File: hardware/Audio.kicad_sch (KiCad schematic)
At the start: 48 parts, among them IC1 LM4991xx, J4 CAT_TX, J6 CAT_TX, Q1 IRLML2060, Q2 BSS138, Q3 BSS138, U1 MAX9814, U201 MCP6002

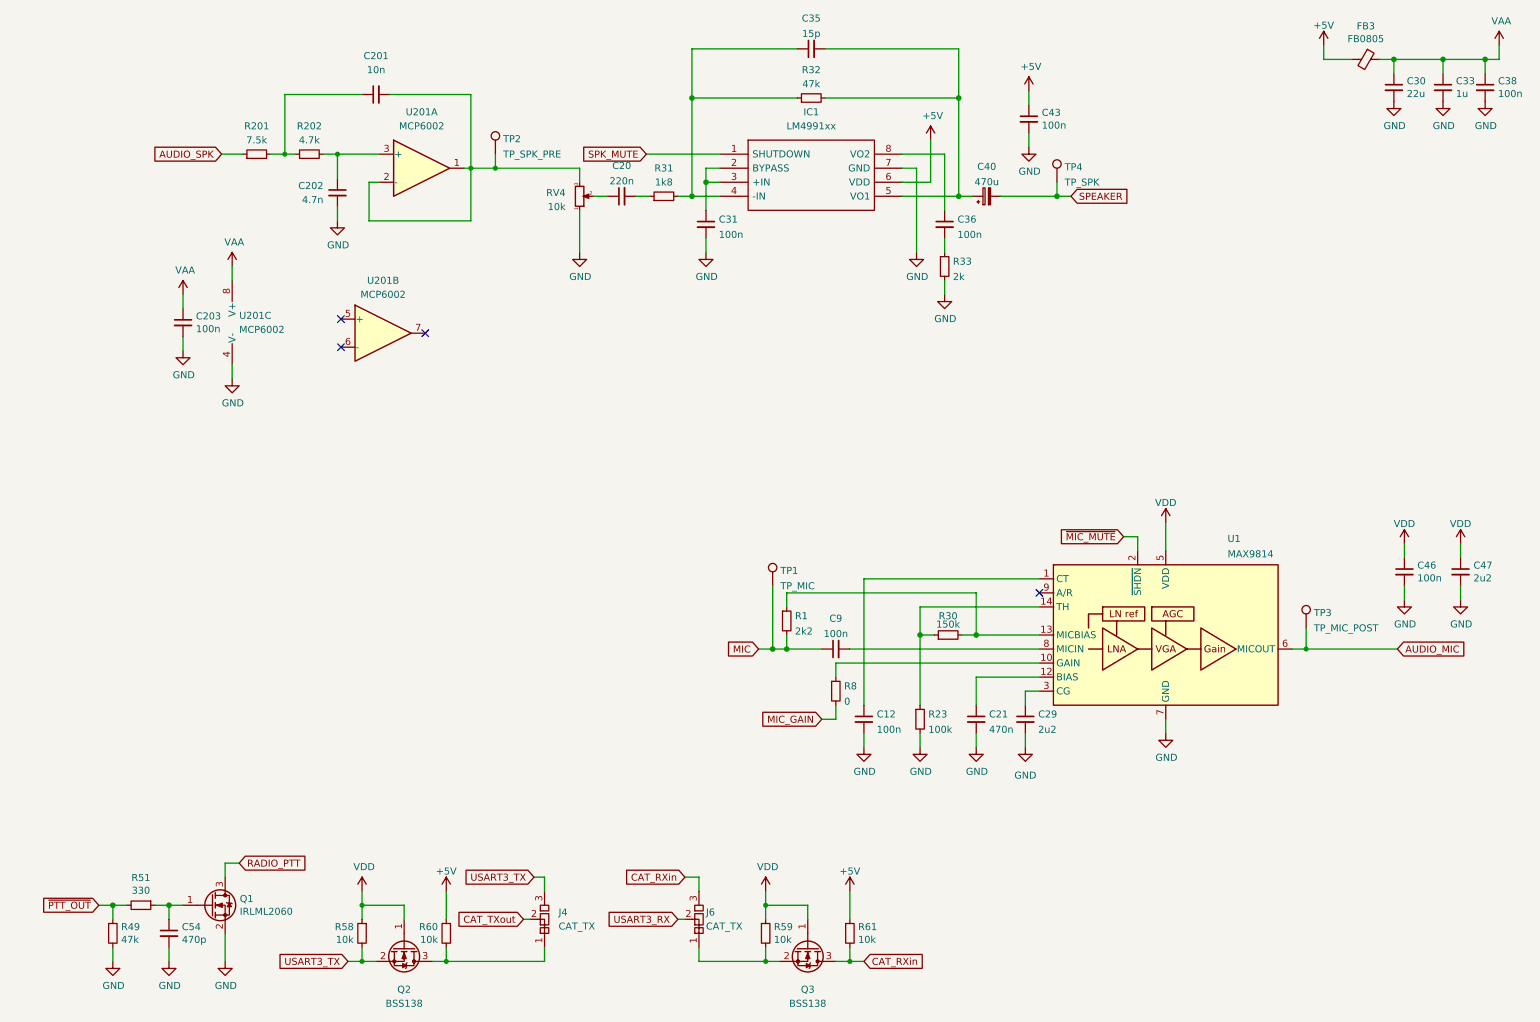
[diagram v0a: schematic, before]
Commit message: Reworked schematic
Rearranged disposition and renumbered components
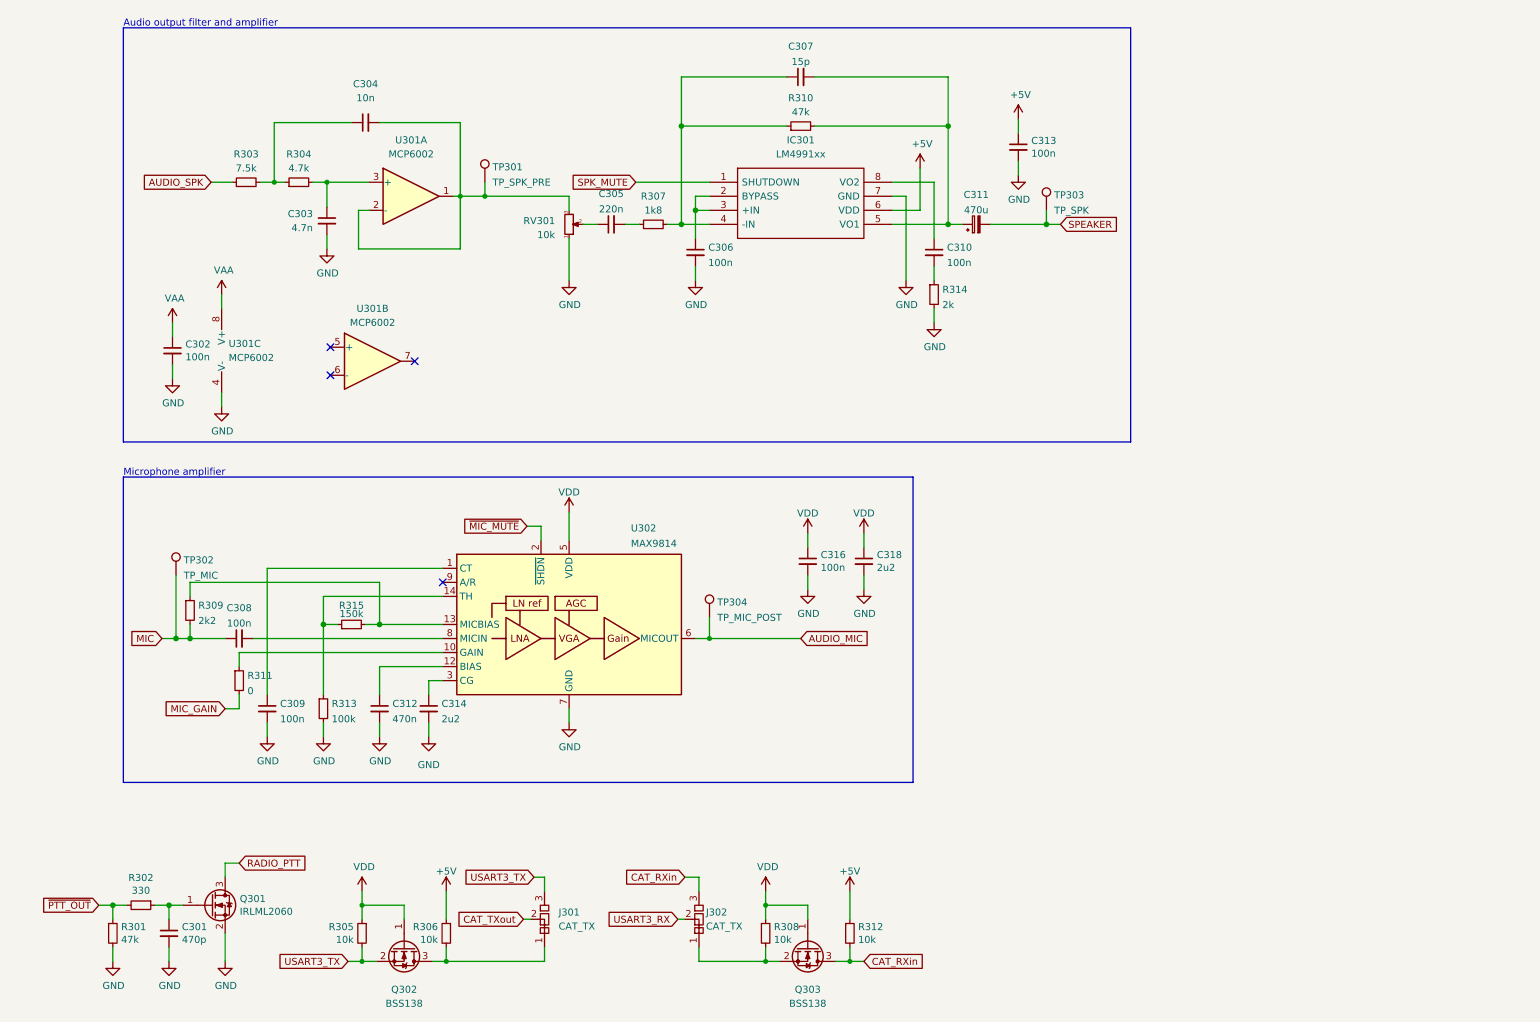
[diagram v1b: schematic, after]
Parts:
- removed C30: 22u, pkl_dipol:C_0603, symbol pkl_device:pkl_C_Small
- removed C33: 1u, pkl_dipol:C_0603, symbol pkl_device:pkl_C_Small
- removed C38: 100n, pkl_dipol:C_0603, symbol pkl_device:pkl_C_Small
- removed FB3: FB0805, pkl_dipol:L_0805, symbol Device:Ferrite_Bead_Small
- renumbered C54 to C301, C203 to C302, C202 to C303, C201 to C304, C20 to C305, C31 to C306, C35 to C307, C9 to C308, C12 to C309, C36 to C310, C40 to C311, C21 to C312, C43 to C313, C29 to C314, C46 to C316, C47 to C318, IC1 to IC301, J4 to J301, J6 to J302, Q1 to Q301, Q2 to Q302, Q3 to Q303, R49 to R301, R51 to R302, R201 to R303, R202 to R304, R58 to R305, R60 to R306, R31 to R307, R59 to R308, R1 to R309, R32 to R310, R8 to R311, R61 to R312, R23 to R313, R33 to R314, R30 to R315, RV4 to RV301, TP2 to TP301, TP1 to TP302, TP4 to TP303, TP3 to TP304, U201 to U301, U1 to U302
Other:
- note added: "Audio output filter and amplifier"
- note added: "Microphone amplifier"
- moved on the sheet: C302, C303, C304, C305, C306, C307, C308, C309, C310, C311, C312, C313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

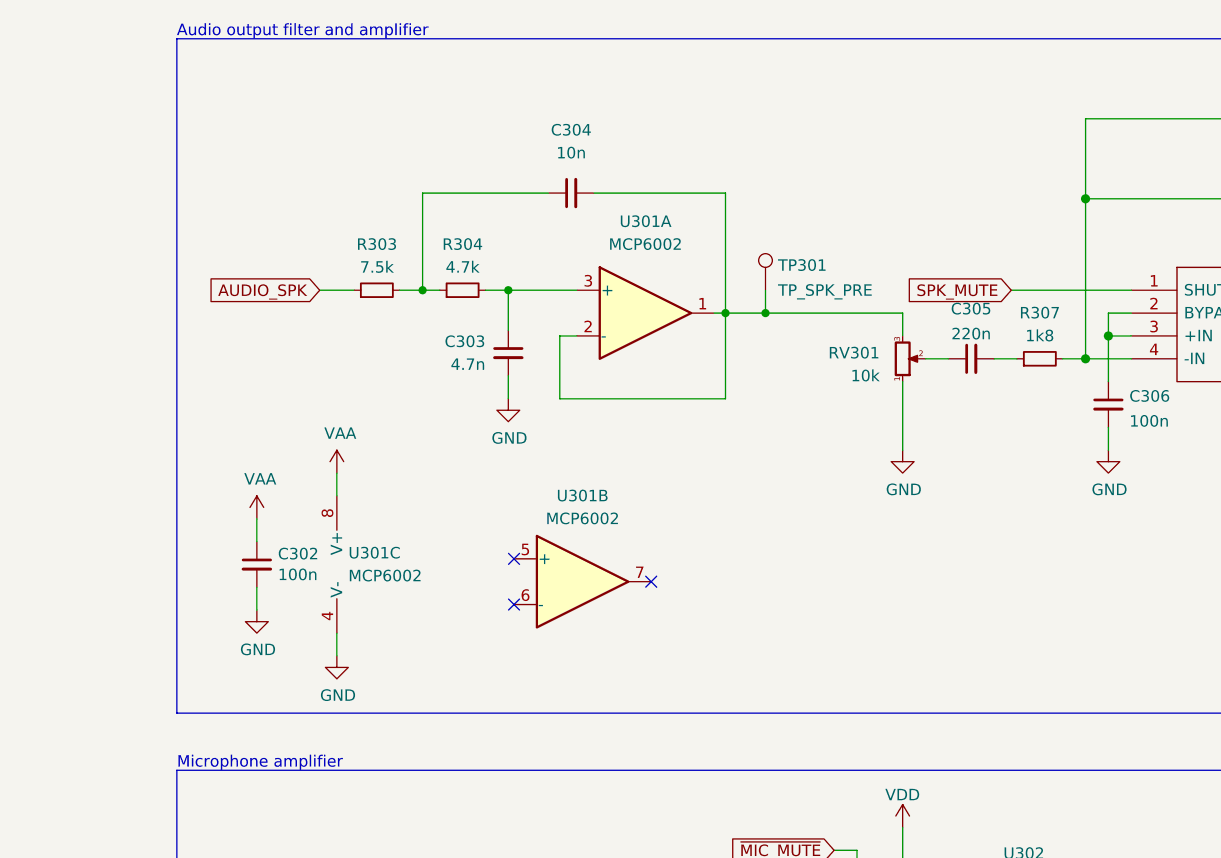
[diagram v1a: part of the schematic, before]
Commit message: Updated audio output stage
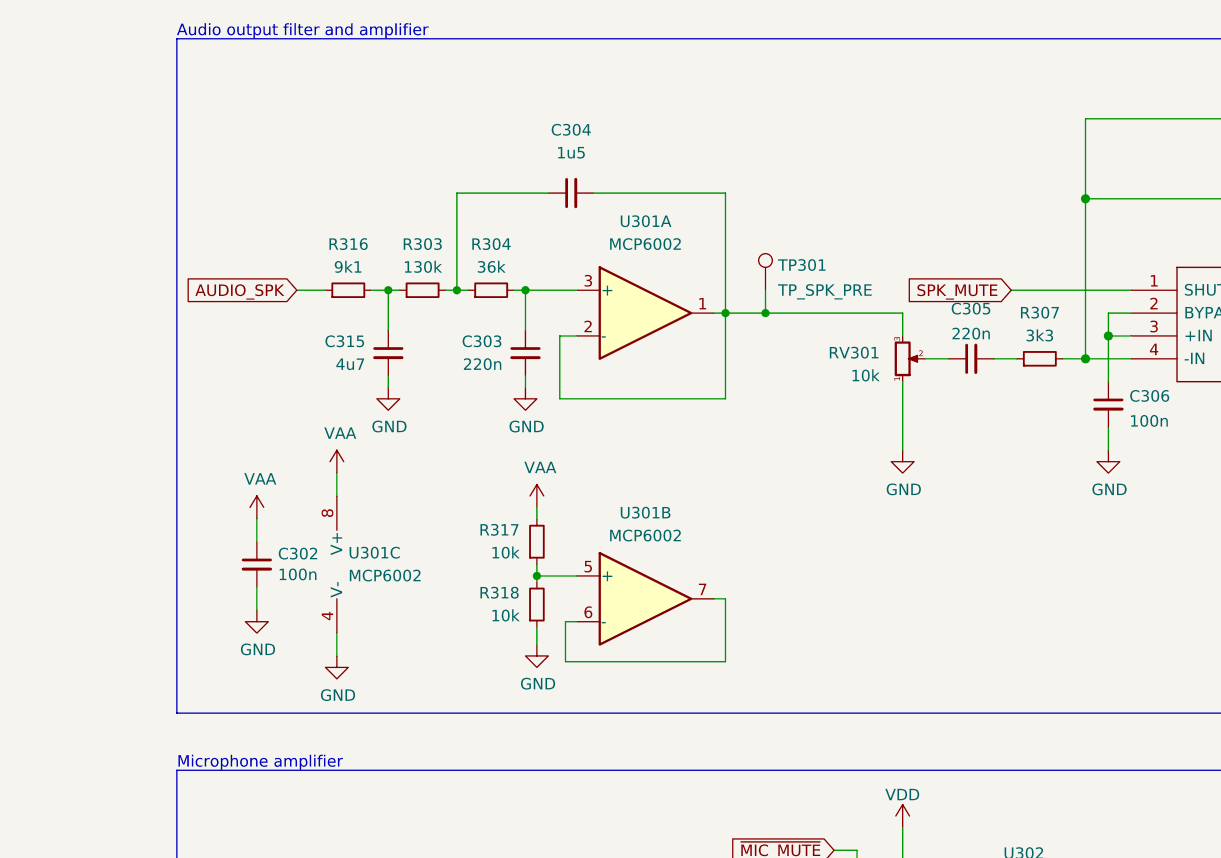
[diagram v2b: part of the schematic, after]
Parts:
- added C315: 4u7, pkl_dipol:C_0603, symbol Device:C_Small
- added R316: 9k1, pkl_dipol:R_0603, symbol Device:R_Small
- added R317, R318: 10k, pkl_dipol:R_0603, symbol Device:R_Small
- C303: value 4.7n -> 220n; MPN (none) -> Generic C 220n/X7R/10V/0603
- C304: value 10n -> 1u5; MPN Generic C/10nF/C0G/25V/0603 -> Generic C 1u5/X7R/10V/0603
- R303: value 7.5k -> 130k; MPN (none) -> Generic R/130k/0603
- R304: value 4.7k -> 36k; MPN (none) -> Generic R/36k/0603
- R307: value 1k8 -> 3k3; MPN Generic R/1k8/0603 -> Generic R/3k3/0603
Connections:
- net AUDIO_SPK: now also R316.1; no longer R303.1
- net GND: now also C315.2, R318.1
- net VAA: now also R317.2
- net at U301.5 (+): now also R317.1, R318.2
- net at U301.6 (-): now also U301.7
- new net: C315.1, R303.1, R316.2
- no-connect marks 4 -> 1
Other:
- moved on the sheet: C303, R303, R304, U301B

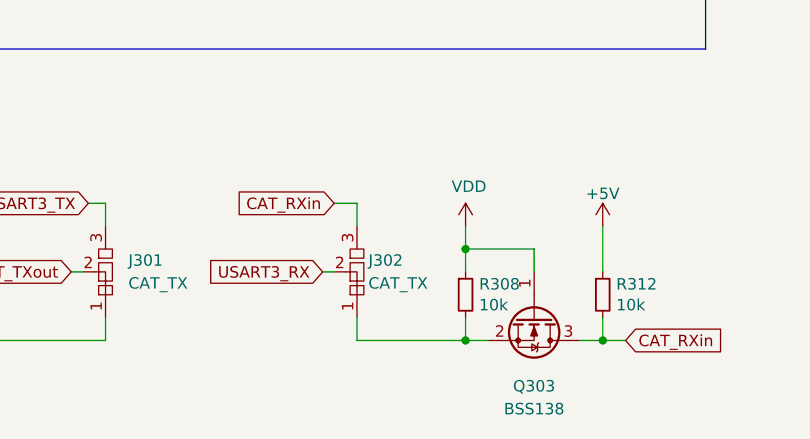
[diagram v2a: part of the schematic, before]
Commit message: Updated bad CAT label
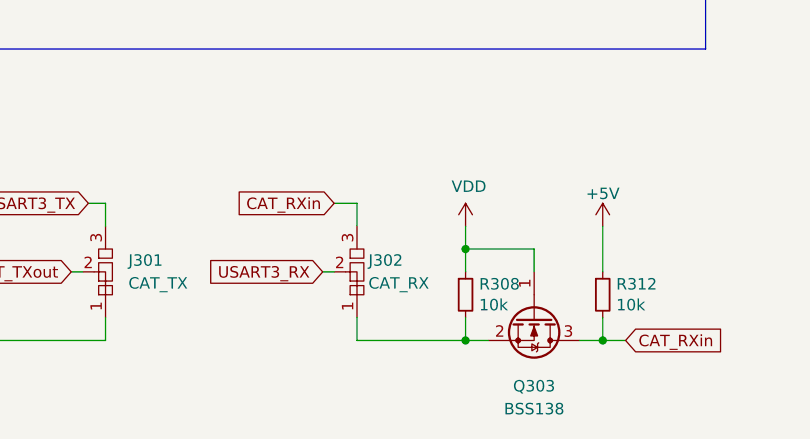
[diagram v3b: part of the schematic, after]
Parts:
- J302: value CAT_TX -> CAT_RX
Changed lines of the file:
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@@
       (effects (font (size 1.27 1.27)) (justify right))
     )
-    (property "Value" "CAT_TX" (at 135.255 181.61 90)
+    (property "Value" "CAT_RX" (at 135.255 181.61 90)
       (effects (font (size 1.27 1.27)) (justify right))
     )

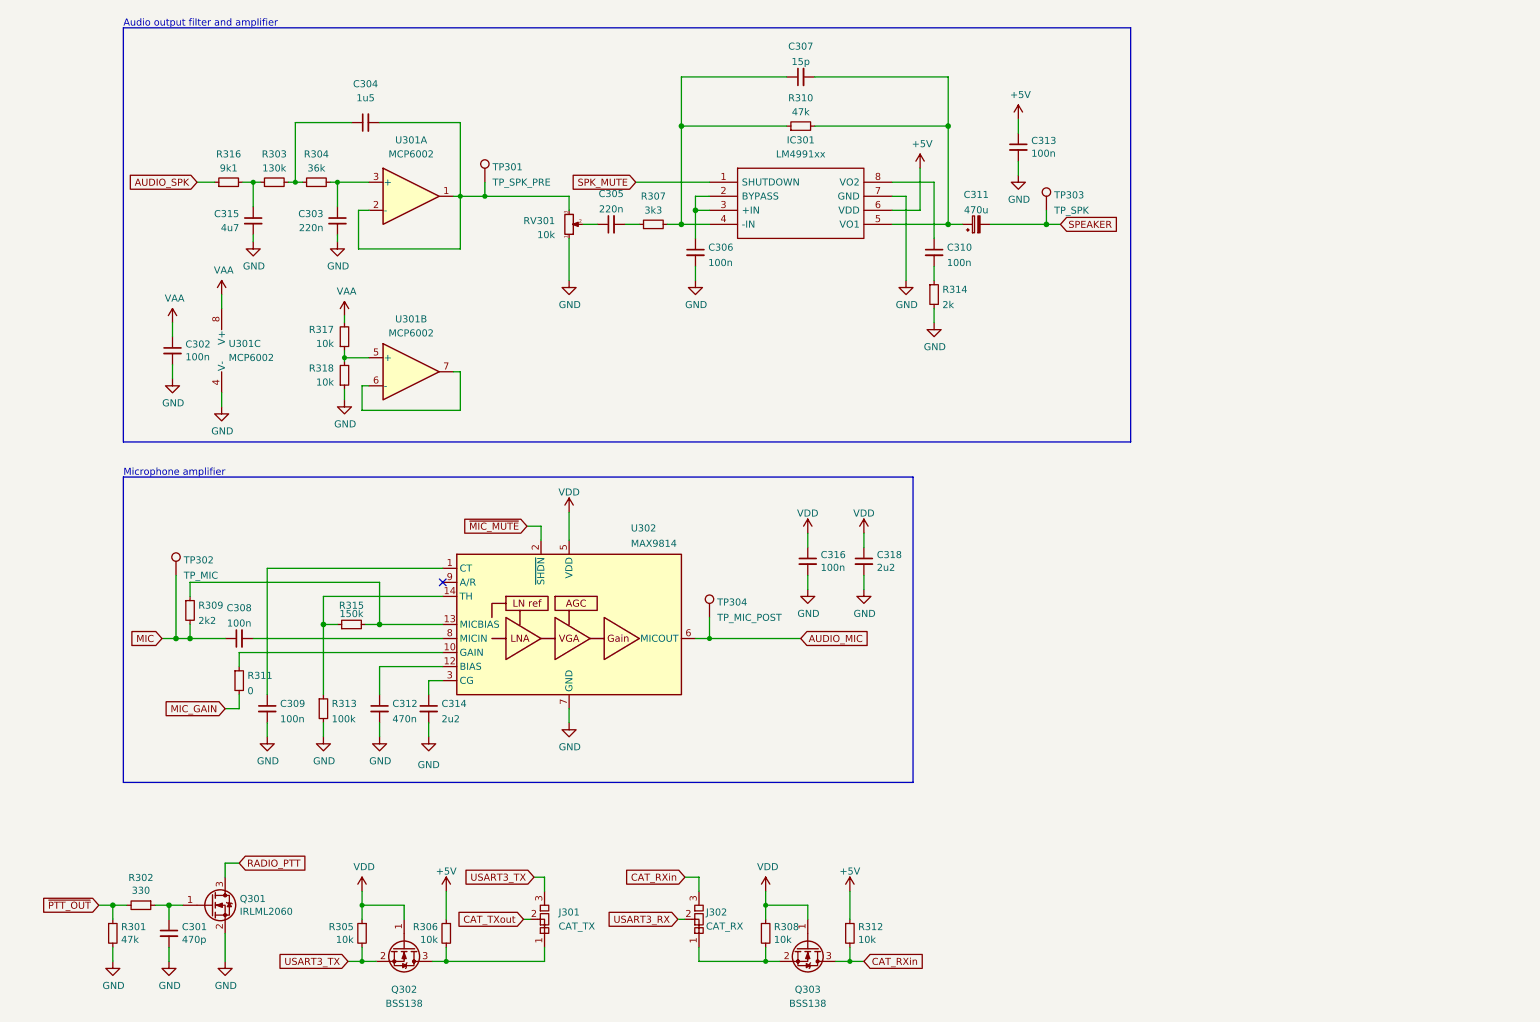
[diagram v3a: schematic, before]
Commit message: Replaced pkl symbols with kicad library symbols
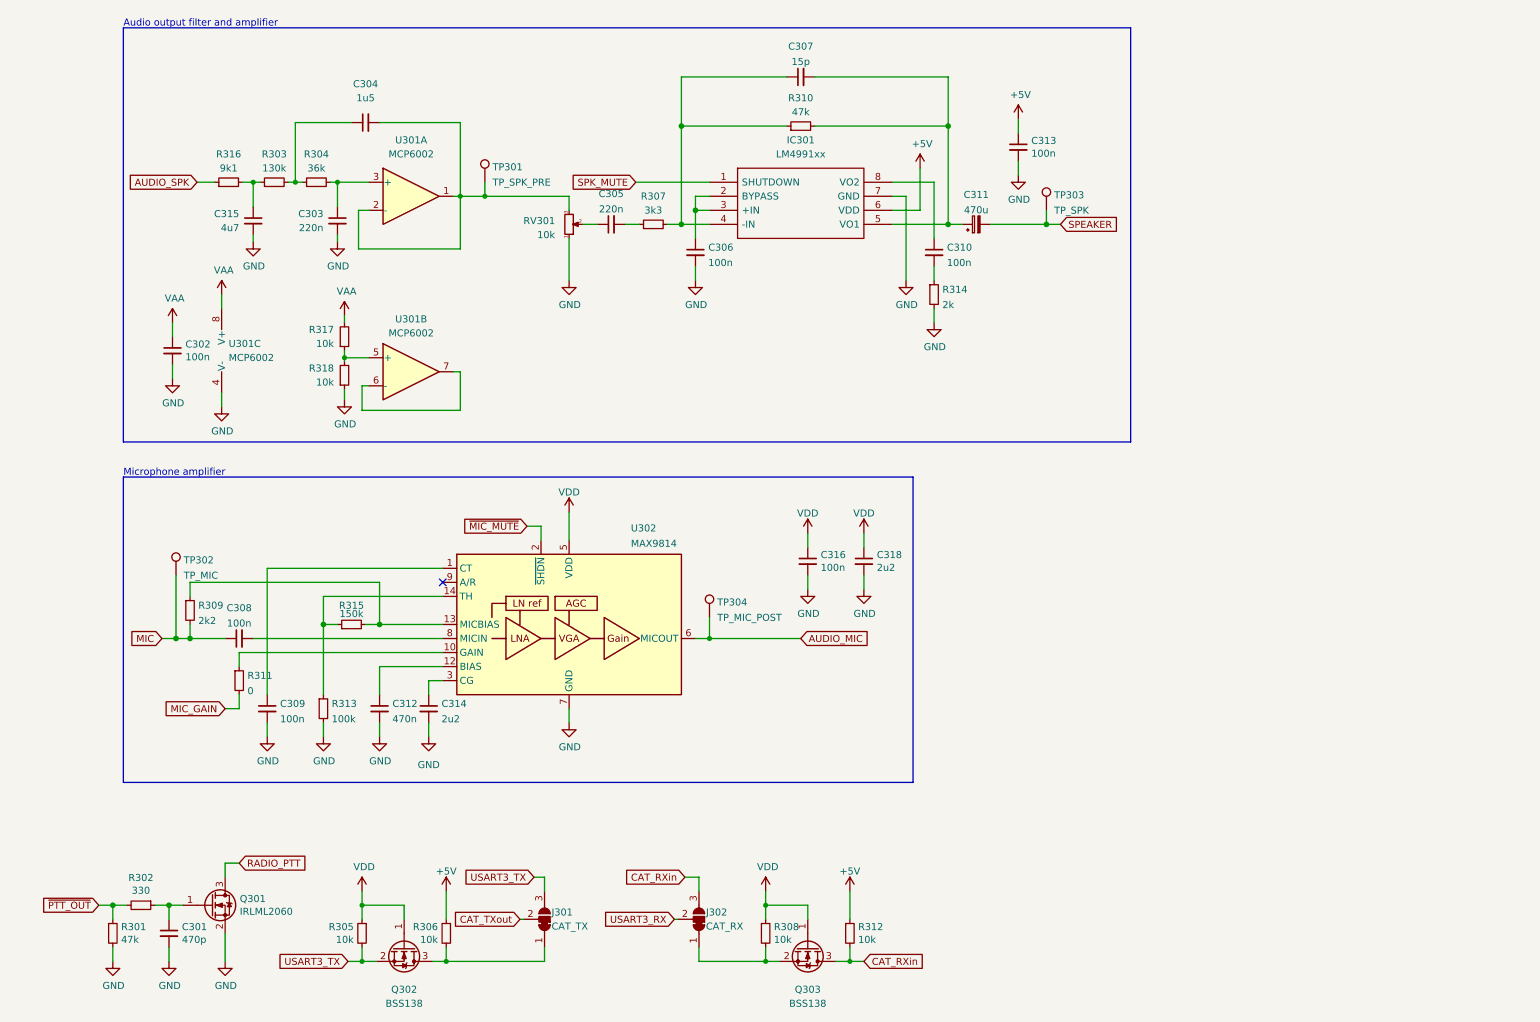
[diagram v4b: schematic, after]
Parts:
- C301, C302, C305, C306, C307, C308, C309, C310, C312, C313, C314, C316, C318: symbol pkl_device:pkl_C_Small -> Device:C_Small
- C311: symbol pkl_device:pkl_CP_Small -> Device:C_Polarized_Small
- J301, J302: symbol pkl_misc:pkl_double_jumper_ncno -> Jumper:SolderJumper_3_Bridged12
- R301, R302, R305, R306, R307, R308, R309, R310, R311, R312, R313, R314, R315: symbol pkl_device:pkl_R_Small -> Device:R_Small
